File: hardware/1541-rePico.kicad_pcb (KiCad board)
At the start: 2 copper layers, 59.1 x 67.3 mm, 13 parts, among them IC2 VIA6522, J1 Display Connector, J2 KEYS, J3 RESET_1541, J4 SD Card Module Connector, J5 EXT_5V, P1 VIA_PIN_1-20, P2 VIA_PIN_21-40, SW1 RESET, U1 Pico

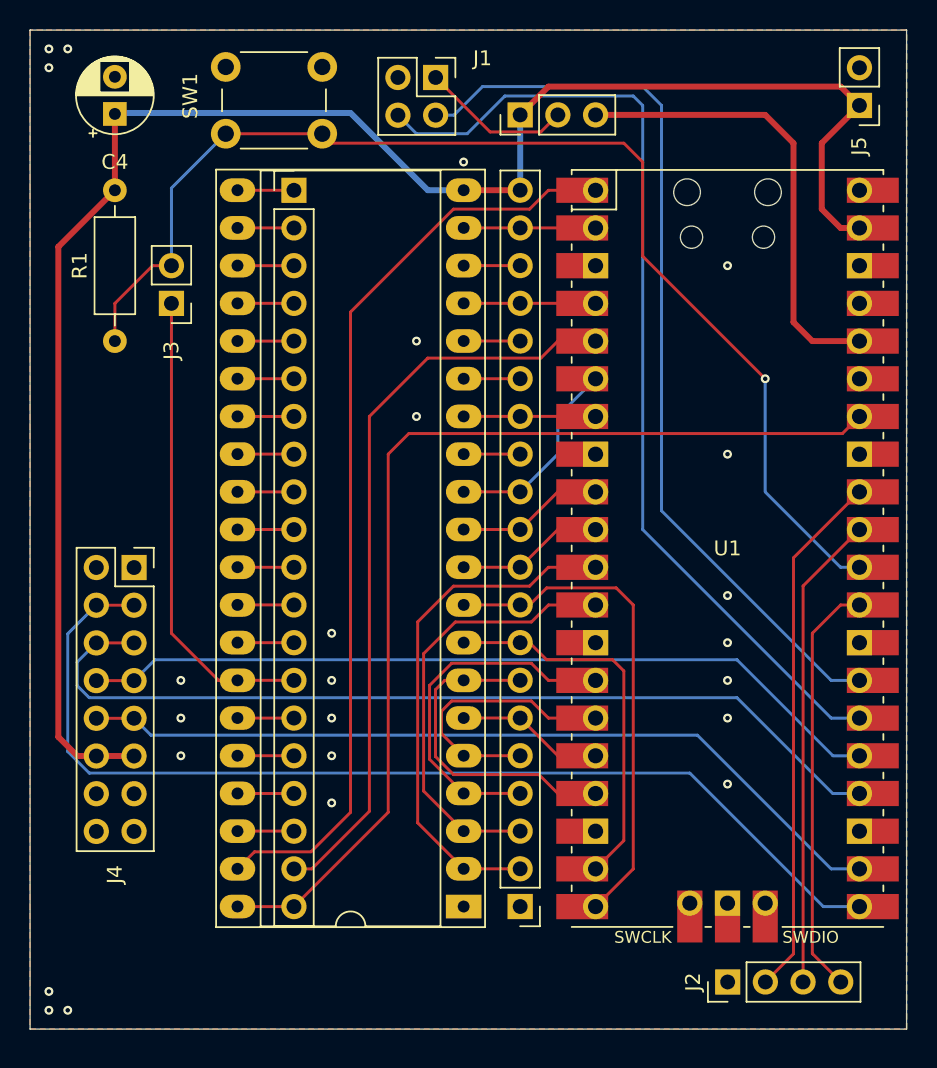
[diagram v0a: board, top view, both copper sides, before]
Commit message: updated PCB layout
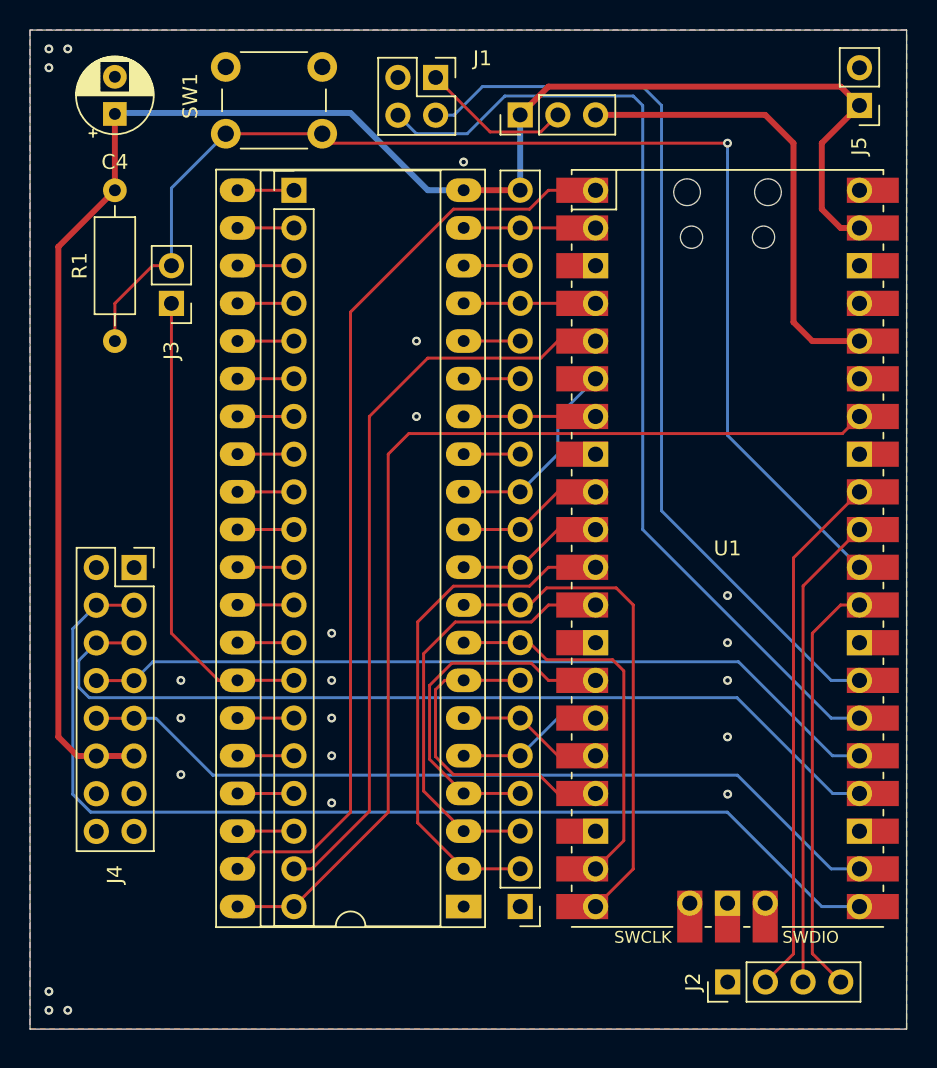
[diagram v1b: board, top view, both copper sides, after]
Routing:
- net /VIA 6522 Sockel/PA3: track 18.6 -> 9.94 mm
- net Net-(J3-Pin_2): track 80.8 -> 84.1 mm
- net SCK: track 61.7 -> 63.4 mm
- net MISO: track 70.9 -> 72.1 mm
- net GND: vias 24 -> 22

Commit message: updated schematics&pcb - version 1.1
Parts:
- J2: value KEYS -> Conn_02x03_Odd_Even; footprint Connector_PinHeader_2.54mm:PinHeader_1x04_P2.54mm_Vertical -> Connector_PinHeader_2.54mm:PinHeader_2x03_P2.54mm_Vertical
- moved J5 73.0 mm to (114.3, 122.7), turned to -90 degrees
- moved J1 67.8 mm to (154.2, 123.3), turned to 180 degrees
- moved Display_Power1 61.1 mm to (118.1, 122.7)
- moved SW1 30.9 mm to (103.9, 89.7), turned to 90 degrees
- moved J2 19.1 mm to (128.1, 123.3)
- moved C4 6.90 mm to (103.8, 70.0)
- moved J3 6.64 mm to (104.0, 79.5)
- moved J4 5.14 mm to (107.2, 99.1)
- moved R1 2.92 mm to (108.4, 80.2)
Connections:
- J2 pad 3: /BT2 -> GND
- J2 pad 4: /BT3 -> /BT2
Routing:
- net +3.3V: track 31.2 -> 118.0 mm
- net I2C_SDA: track 67.0 -> 19.1 mm
- net I2C_SCL: track 61.9 -> 21.8 mm
- net Net-(Display_Power1-Pin_2): track 10.9 -> 36.9 mm
- net Net-(J3-Pin_2): track 84.1 -> 64.6 mm, vias 1 -> 0
- net /BT3: track 28.3 -> 44.9 mm
- net /BT2: track 32.1 -> 45.3 mm
- net /BT1: track 35.6 -> 48.7 mm
- net GND: track 0.27 -> 5.08 mm, vias 22 -> 30
- net +5V: track 119.1 -> 122.1 mm
- net SCK: track 63.4 -> 60.8 mm
- net CS: track 55.6 -> 53.5 mm
- net MISO: track 72.1 -> 70.2 mm
- net /VIA 6522 Sockel/~{RESET}: track 31.8 -> 30.0 mm
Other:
- board size 59.1 x 67.3 mm -> 59.1 x 60 mm

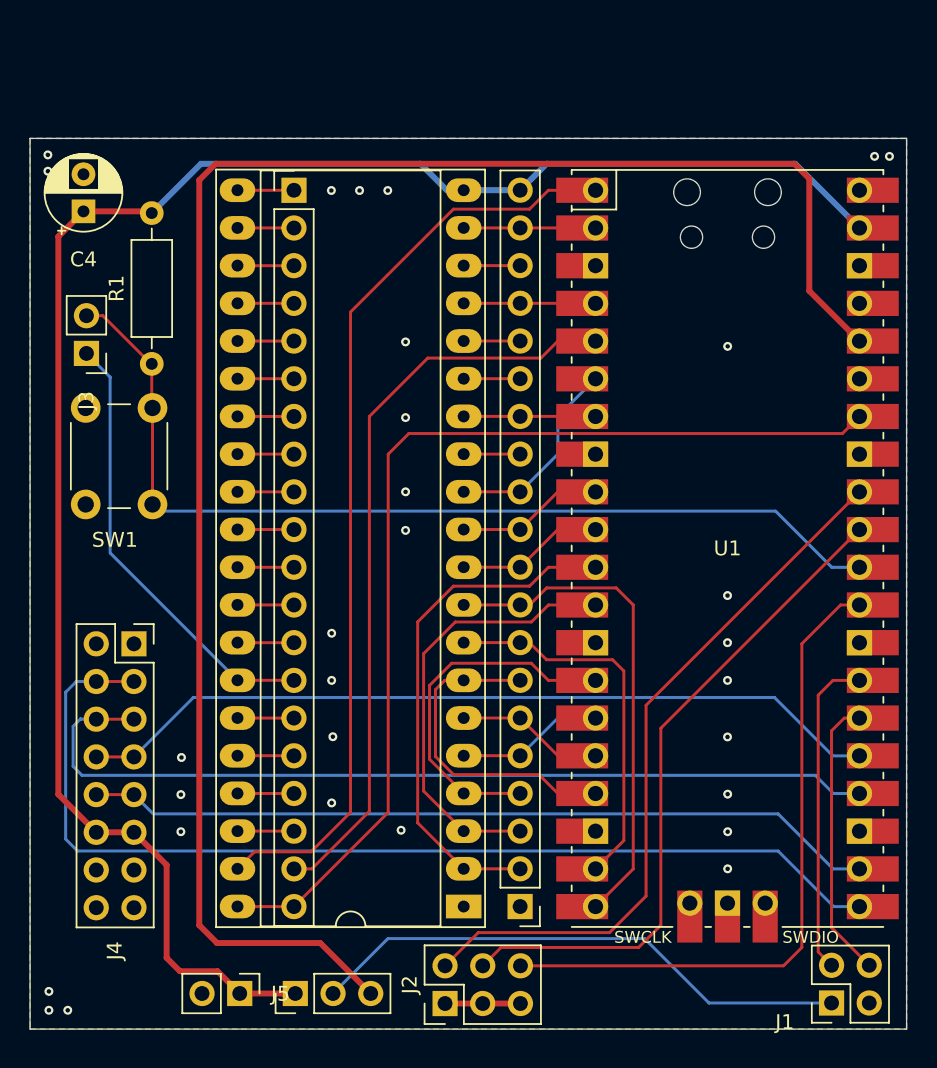
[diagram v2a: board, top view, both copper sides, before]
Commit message: fix WPS cross-driving
connection between 1541-board and VIA cut off
no cross driving of existing 74LS04 and Pico avoided
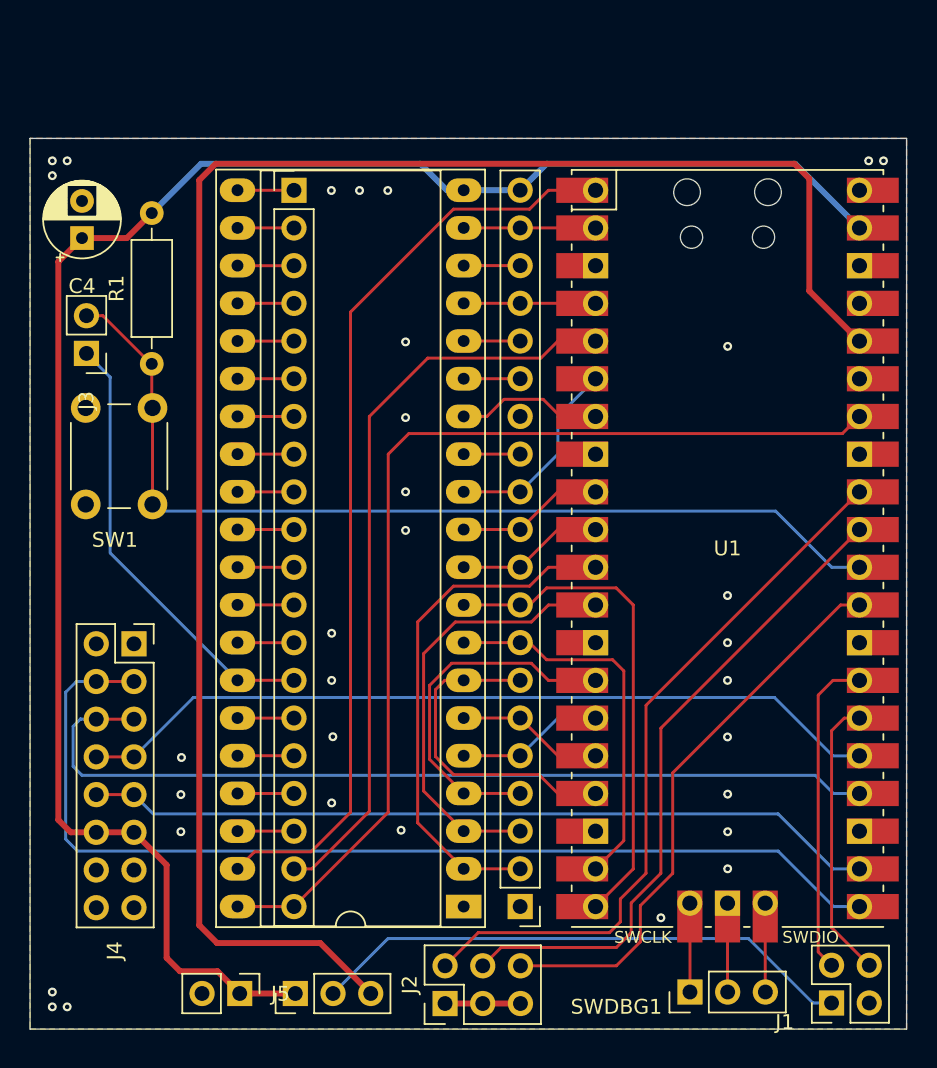
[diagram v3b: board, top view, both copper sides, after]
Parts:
- added SWDBG1: DEBUG, Connector_PinHeader_2.54mm:PinHeader_1x03_P2.54mm_Vertical, F.Cu at (144.6, 122.6)
- moved C4 1.80 mm to (103.7, 71.8)
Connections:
- P1 pad 14: /VIA 6522 Sockel/WPS -> unconnected-(P1-Pin_14-Pad14)
- U1 pad 41: unconnected-(U1-SWCLK-Pad41) -> Net-(SWDBG1-Pin_1)
- U1 pad 42: unconnected-(U1-GND-Pad42) -> Net-(SWDBG1-Pin_2)
- U1 pad 43: unconnected-(U1-SWDIO-Pad43) -> Net-(SWDBG1-Pin_3)
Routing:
- net /BT3: track 44.9 -> 38.3 mm
- net Net-(SWDBG1-Pin_2): track 0.00 -> 5.99 mm
- net Net-(SWDBG1-Pin_3): track 0.00 -> 5.99 mm
- net Net-(SWDBG1-Pin_1): track 0.00 -> 5.99 mm
- net /VIA 6522 Sockel/WPS: track 8.89 -> 9.85 mm
- net /BT2: track 45.3 -> 44.5 mm
- net GND: vias 30 -> 32
